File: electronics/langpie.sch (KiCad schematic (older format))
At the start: 13 parts

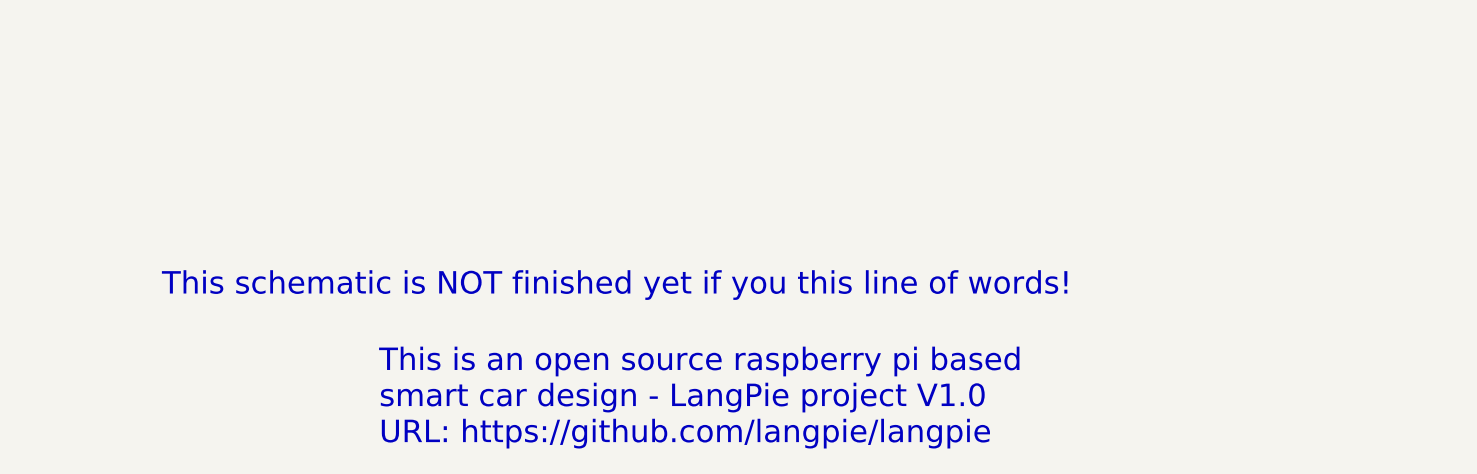
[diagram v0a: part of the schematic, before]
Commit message: Electronics define IOs to motor driver.
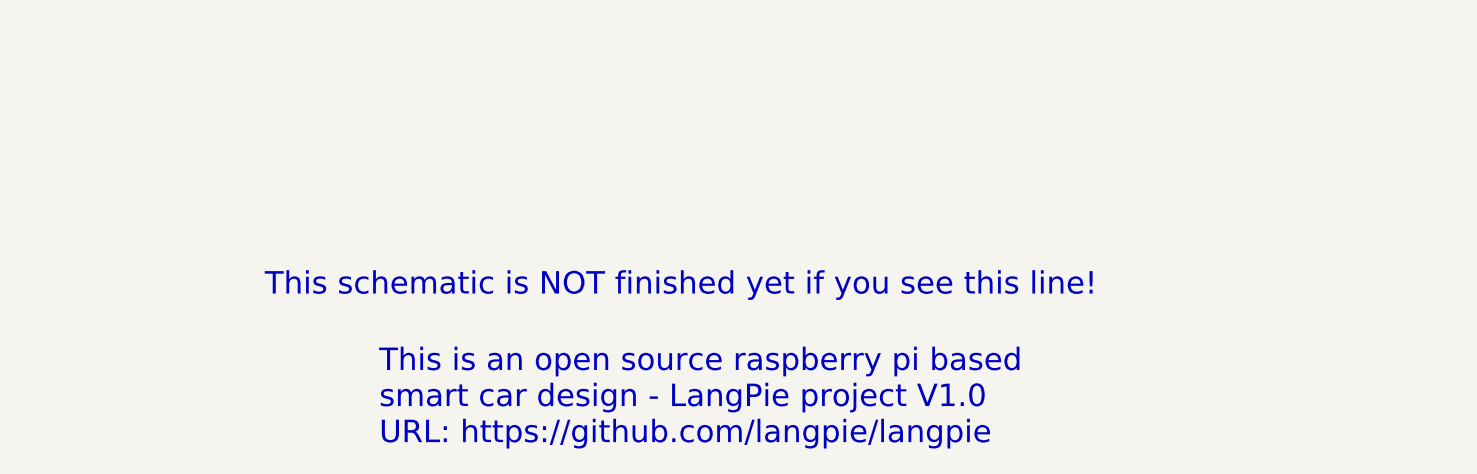
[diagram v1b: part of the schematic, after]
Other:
- note added: "This schematic is NOT finished yet if you see this line!\n"
- note removed: "This schematic is NOT finished yet if you this line of words!\n"
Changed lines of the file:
@@
 Text Notes 7450 7050 0    98   ~ 0
 This is an open source raspberry pi based \nsmart car design - LangPie project V1.0\nURL: https://github.com/langpie/langpie
-Text Notes 6500 6400 0    98   ~ 0
-This schematic is NOT finished yet if you this line of words!\n
+Text Notes 6950 6400 0    98   ~ 0
+This schematic is NOT finished yet if you see this line!\n
 $Sheet
 S 4600 2300 1000 1000

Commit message: modified:   ../../electronics/charger.sch 	modified:   ../../electronics/charger.sch-bak 	modified:   ../../electronics/dc_dc.sch 	modified:   ../../electronics/dc_dc.sch-bak 	modified:   ../../electronics/langpie.pro 	modified:   ../../electronics/langpie.sch 	modified:   ../../electronics/langpie.sch-bak 	modified:   ../../electronics/motor_driver_rpi_pi.sch 	modified:   ../../electronics/motor_driver_rpi_pi.sch-bak 	modified:   ../../electronics/schematic_v1_preview.pdf
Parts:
- gave numbers to parts that had none: 13
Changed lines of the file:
@@
 P 3100 4800
 AR Path="/5E90B2B2/5EAD01BB" Ref="Q?"  Part="1"
-AR Path="/5EAD01BB" Ref="Q?"  Part="1"
-F 0 "Q?" H 3300 4650 50  0000 L CNN
+AR Path="/5EAD01BB" Ref="Q1"  Part="1"
+F 0 "Q1" H 3300 4650 50  0000 L CNN
 F 1 "2N7000" H 3300 4550 50  0000 L CNN
 F 2 "Package_TO_SOT_SMD:SOT-23" H 3300 4725 50  0001 L CIN
@@
 P 2550 4800
 AR Path="/5E90B2B2/5EAD01C9" Ref="R?"  Part="1"
-AR Path="/5EAD01C9" Ref="R?"  Part="1"
-F 0 "R?" V 2757 4800 50  0000 C CNN
+AR Path="/5EAD01C9" Ref="R1"  Part="1"
+F 0 "R1" V 2757 4800 50  0000 C CNN
 F 1 "1K" V 2666 4800 50  0000 C CNN
 F 2 "Resistor_SMD:R_0805_2012Metric" V 2480 4800 50  0001 C CNN
@@
 P 2800 5100
 AR Path="/5E90B2B2/5EAD01CF" Ref="R?"  Part="1"
-AR Path="/5EAD01CF" Ref="R?"  Part="1"
-F 0 "R?" H 2870 5146 50  0000 L CNN
+AR Path="/5EAD01CF" Ref="R2"  Part="1"
+F 0 "R2" H 2870 5146 50  0000 L CNN
 F 1 "47K" H 2870 5055 50  0000 L CNN
 F 2 "Resistor_SMD:R_0805_2012Metric" V 2730 5100 50  0001 C CNN
@@
 P 2350 2700
 AR Path="/5E915994/5EAD66D6" Ref="J?"  Part="1"
-AR Path="/5EAD66D6" Ref="J?"  Part="1"
-F 0 "J?" H 2407 3167 50  0000 C CNN
+AR Path="/5EAD66D6" Ref="J1"  Part="1"
+F 0 "J1" H 2407 3167 50  0000 C CNN
 F 1 "USB_B_Micro" H 2407 3076 50  0000 C CNN
 F 2 "Connector_USB:USB_Micro-B_GCT_USB3076-30-A" H 2500 2650 50  0001 C CNN
@@
 P 8300 3600
 AR Path="/5E914BA5/5EAE307F" Ref="J?"  Part="1"
-AR Path="/5EAE307F" Ref="J?"  Part="1"
-F 0 "J?" H 8380 3592 50  0000 L CNN
+AR Path="/5EAE307F" Ref="J3"  Part="1"
+F 0 "J3" H 8380 3592 50  0000 L CNN
 F 1 "Conn_01x02" H 8380 3501 50  0000 L CNN
 F 2 "Connector_Wire:SolderWirePad_1x02_P5.08mm_Drill1.5mm" H 8300 3600 50  0001 C CNN
@@
 P 8300 3900
 AR Path="/5E914BA5/5EAE3085" Ref="J?"  Part="1"
-AR Path="/5EAE3085" Ref="J?"  Part="1"
-F 0 "J?" H 8380 3892 50  0000 L CNN
+AR Path="/5EAE3085" Ref="J4"  Part="1"
+F 0 "J4" H 8380 3892 50  0000 L CNN
 F 1 "Conn_01x02" H 8380 3801 50  0000 L CNN
 F 2 "Connector_Wire:SolderWirePad_1x02_P5.08mm_Drill1.5mm" H 8300 3900 50  0001 C CNN
@@
 $EndComp
 $Comp
-L Device:Fuse F?
+L Device:Fuse F1
 U 1 1 5EAF3CDE
 P 3550 2500
-F 0 "F?" V 3353 2500 50  0000 C CNN
+F 0 "F1" V 3353 2500 50  0000 C CNN
 F 1 "Fuse" V 3444 2500 50  0000 C CNN
 F 2 "Fuse:Fuse_1206_3216Metric" V 3480 2500 50  0001 C CNN
@@
 $EndComp
 $Comp
-L Switch:SW_SPDT SW?
+L Switch:SW_SPDT SW1
 U 1 1 5EAF599A
 P 3650 4600
-F 0 "SW?" H 3650 4885 50  0000 C CNN
+F 0 "SW1" H 3650 4885 50  0000 C CNN
 F 1 "SW_SPDT" H 3650 4794 50  0000 C CNN
 F 2 "" H 3650 4600 50  0001 C CNN
@@
 $EndComp
 $Comp
-L Connector_Generic:Conn_01x04 J?
+L Connector_Generic:Conn_01x04 J2
 U 1 1 5EBABE63
 P 8300 3150
-F 0 "J?" H 8380 3142 50  0000 L CNN
+F 0 "J2" H 8380 3142 50  0000 L CNN
 F 1 "Conn_01x04" H 8380 3051 50  0000 L CNN
 F 2 "Connector_PinHeader_2.54mm:PinHeader_1x04_P2.54mm_Vertical" H 8300 3150 50  0001 C CNN
@@
 P 4050 2750
 AR Path="/5E90B2B2/5EBDCC0E" Ref="R?"  Part="1"
-AR Path="/5EBDCC0E" Ref="R?"  Part="1"
-F 0 "R?" H 4120 2796 50  0000 L CNN
+AR Path="/5EBDCC0E" Ref="R4"  Part="1"
+F 0 "R4" H 4120 2796 50  0000 L CNN
 F 1 "1K" H 4120 2705 50  0000 L CNN
 F 2 "Resistor_SMD:R_0805_2012Metric" V 3980 2750 50  0001 C CNN
@@
 P 4050 3100
 AR Path="/5E90B2B2/5EBDCC14" Ref="D?"  Part="1"
-AR Path="/5EBDCC14" Ref="D?"  Part="1"
-F 0 "D?" V 4089 2983 50  0000 R CNN
+AR Path="/5EBDCC14" Ref="D1"  Part="1"
+F 0 "D1" V 4089 2983 50  0000 R CNN
 F 1 "LED" V 3998 2983 50  0000 R CNN
 F 2 "LED_SMD:LED_0805_2012Metric" H 4050 3100 50  0001 C CNN
@@
 P 3200 4150
 AR Path="/5E90B2B2/5EBEA222" Ref="R?"  Part="1"
-AR Path="/5EBEA222" Ref="R?"  Part="1"
-F 0 "R?" V 3407 4150 50  0000 C CNN
+AR Path="/5EBEA222" Ref="R3"  Part="1"
+F 0 "R3" V 3407 4150 50  0000 C CNN
 F 1 "10K" V 3316 4150 50  0000 C CNN
 F 2 "Resistor_SMD:R_0805_2012Metric" V 3130 4150 50  0001 C CNN
@@
 This connects to 18650*2 batteries (8.4V)
 $Comp
-L Device:Battery BT?
+L Device:Battery BT1
 U 1 1 5EBFE8F3
 P 2700 3800
-F 0 "BT?" V 3000 3650 50  0000 L CNN
+F 0 "BT1" V 3000 3650 50  0000 L CNN
 F 1 "LiBattery" V 2900 3650 50  0000 L CNN
 F 2 "" V 2700 3860 50  0001 C CNN

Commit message: update pcb file and netlist
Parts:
- BT1: footprint (none) -> Connector_Wire:SolderWirePad_1x02_P5.08mm_Drill1.5mm
- SW1: footprint (none) -> Button_Switch_THT:SW_CuK_OS102011MA1QN1_SPDT_Angled
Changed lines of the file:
@@
 F 0 "SW1" H 3650 4885 50  0000 C CNN
 F 1 "SW_SPDT" H 3650 4794 50  0000 C CNN
-F 2 "" H 3650 4600 50  0001 C CNN
+F 2 "Button_Switch_THT:SW_CuK_OS102011MA1QN1_SPDT_Angled" H 3650 4600 50  0001 C CNN
 F 3 "~" H 3650 4600 50  0001 C CNN
 	1    3650 4600
@@
 F 0 "BT1" V 3000 3650 50  0000 L CNN
 F 1 "LiBattery" V 2900 3650 50  0000 L CNN
-F 2 "" V 2700 3860 50  0001 C CNN
+F 2 "Connector_Wire:SolderWirePad_1x02_P5.08mm_Drill1.5mm" V 2700 3860 50  0001 C CNN
 F 3 "~" V 2700 3860 50  0001 C CNN
 	1    2700 3800

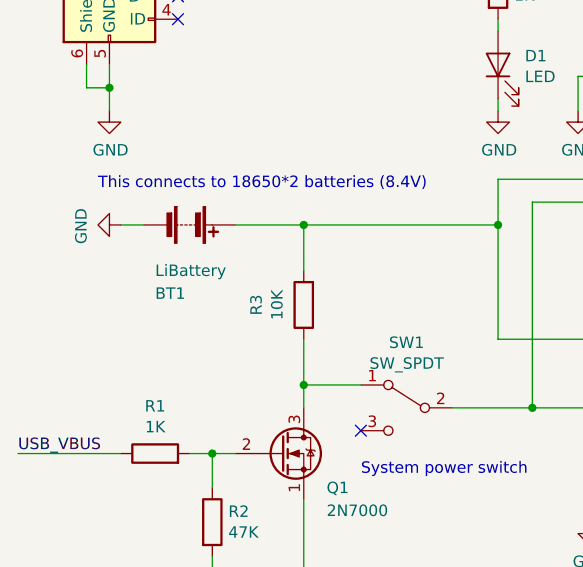
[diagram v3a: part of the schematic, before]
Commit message: Adding PCB and PCB library
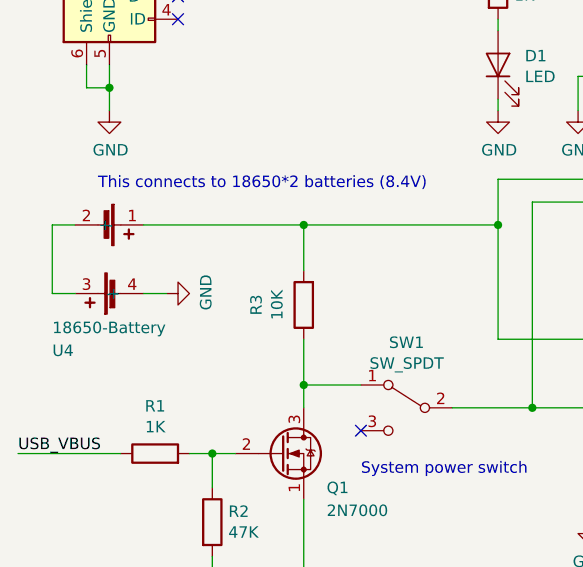
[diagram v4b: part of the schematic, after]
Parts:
- removed BT1: LiBattery, Connector_Wire:SolderWirePad_1x02_P5.08mm_Drill1.5mm, symbol Device:Battery
- added U4: 18650-Battery, langpie:li-battery-case, symbol langpie:18650-Battery
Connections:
- net Battery Charger/BATT: now also U4.1 (+)
- net GND: now also U4.4 (-)
- new net: U4.2 (-), U4.3 (+)
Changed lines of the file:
@@
 L power:GND #PWR?
 U 1 1 5EBC675D
-P 2400 3800
+P 2600 4100
 AR Path="/5E90B2B2/5EBC675D" Ref="#PWR?"  Part="1"
 AR Path="/5EBC675D" Ref="#PWR0107"  Part="1"
-F 0 "#PWR0107" H 2400 3550 50  0001 C CNN
-F 1 "GND" H 2405 3627 50  0000 C CNN
-F 2 "" H 2400 3800 50  0001 C CNN
-F 3 "" H 2400 3800 50  0001 C CNN
-	1    2400 3800
-	0    1    1    0
+F 0 "#PWR0107" H 2600 3850 50  0001 C CNN
+F 1 "GND" H 2605 3927 50  0000 C CNN
+F 2 "" H 2600 4100 50  0001 C CNN
+F 3 "" H 2600 4100 50  0001 C CNN
+	1    2600 4100
+	0    -1   -1   0
 $EndComp
-Wire Wire Line
-	2900 3800 3200 3800
 Connection ~ 5750 3350
 $Comp
@@
 This connects to 18650*2 batteries (8.4V)
 $Comp
-L Device:Battery BT1
-U 1 1 5EBFE8F3
-P 2700 3800
-F 0 "BT1" V 3000 3650 50  0000 L CNN
-F 1 "LiBattery" V 2900 3650 50  0000 L CNN
-F 2 "Connector_Wire:SolderWirePad_1x02_P5.08mm_Drill1.5mm" V 2700 3860 50  0001 C CNN
-F 3 "~" V 2700 3860 50  0001 C CNN
-	1    2700 3800
-	0    1    1    0
-$EndComp
-Wire Wire Line
-	2500 3800 2400 3800
-$Comp
 L power:GND #PWR?
 U 1 1 5EC0F274
@@
 F4 "GND" I L 4600 3150 50
 $EndSheet
+$Comp
+L langpie:18650-Battery U4
+U 1 1 5E9C43B4
+P 2900 3650
+F 0 "U4" V 3600 2850 50  0000 L CNN
+F 1 "18650-Battery" V 3500 2850 50  0000 L CNN
+F 2 "langpie:li-battery-case" H 2900 3600 98  0001 C CNN
+F 3 "https://item.taobao.com/item.htm?spm=a230r.1.14.28.2b96113cbFAeSg&id=611774097578&ns=1&abbucket=2#detail" H 2900 3600 98  0001 C CNN
+	1    2900 3650
+	0    1    1    0
+$EndComp
+Wire Wire Line
+	2500 3800 3200 3800
+Wire Wire Line
+	2200 3800 2100 3800
+Wire Wire Line
+	2100 3800 2100 4100
+Wire Wire Line
+	2100 4100 2200 4100
+Wire Wire Line
+	2500 4100 2600 4100
 $EndSCHEMATC

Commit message: Finish PCB, silightly change to SCH, Gerber generated, V1.0 HW almost done.
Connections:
- net Battery Charger/VBUS is gone; now on net USB_VBUS: F1.1, R4.1
- net USB_VBUS: no longer F1.2, J1.1 (VBUS)
- new net: F1.2, J1.1 (VBUS)
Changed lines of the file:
@@
 	0    -1   -1   0
 $EndComp
-Text Notes 3700 2450 0    50   ~ 0
+Text Notes 3700 2400 0    50   ~ 0
 USB voltage input \n    status LED
 $Comp
@@
 Text Label 1950 4800 0    50   ~ 0
 USB_VBUS
-Text Label 2850 2500 0    50   ~ 0
+Text Label 3700 2500 0    50   ~ 0
 USB_VBUS
 Wire Wire Line
